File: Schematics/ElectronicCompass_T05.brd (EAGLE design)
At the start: 50.5 x 50.8 mm, 61 parts, among them Q1 FDN360P, Q2 FDN360P, Q3 FDN360P, Q4 FDN360P, U1 ATMEGA32U4, X1 USBSMD, Y1 16MHz

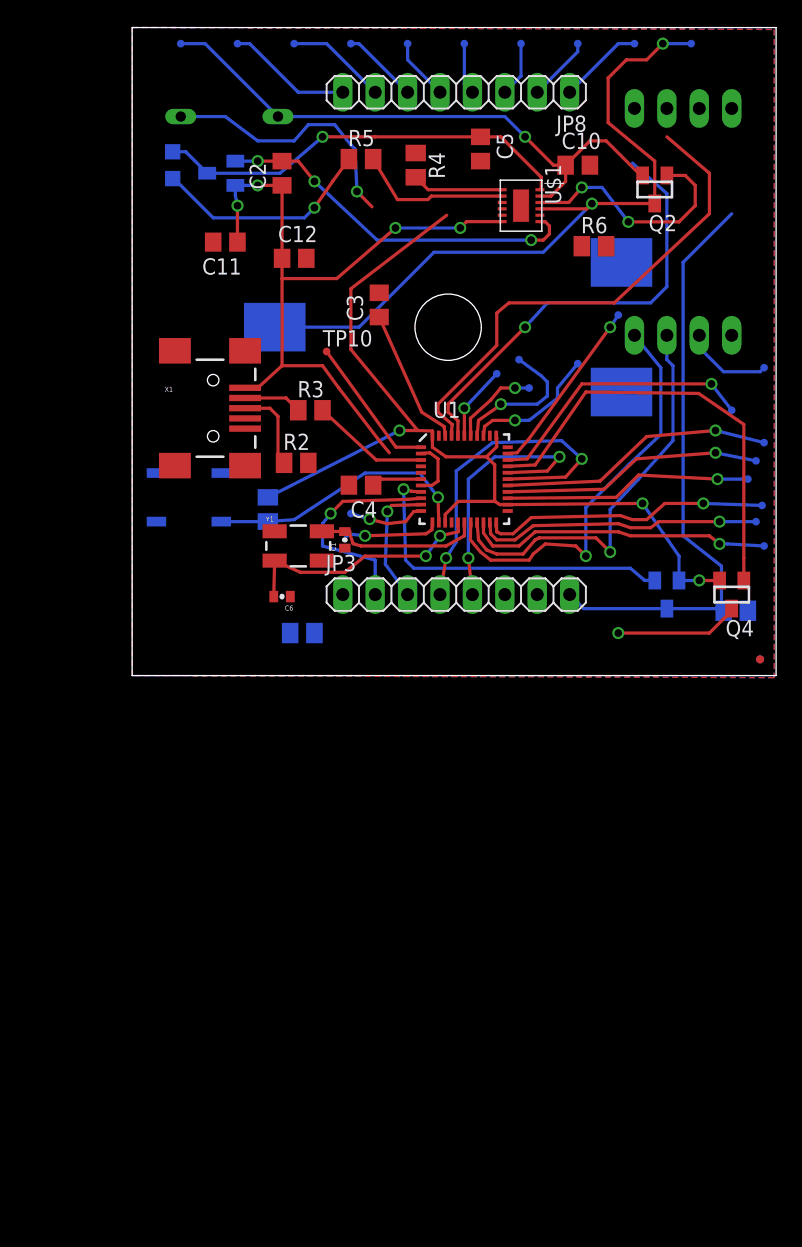
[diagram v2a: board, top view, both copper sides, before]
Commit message: Made some more updates to the schematic according to what Andrew suggested. Still need to put in the new batter header and then fix the board layout.
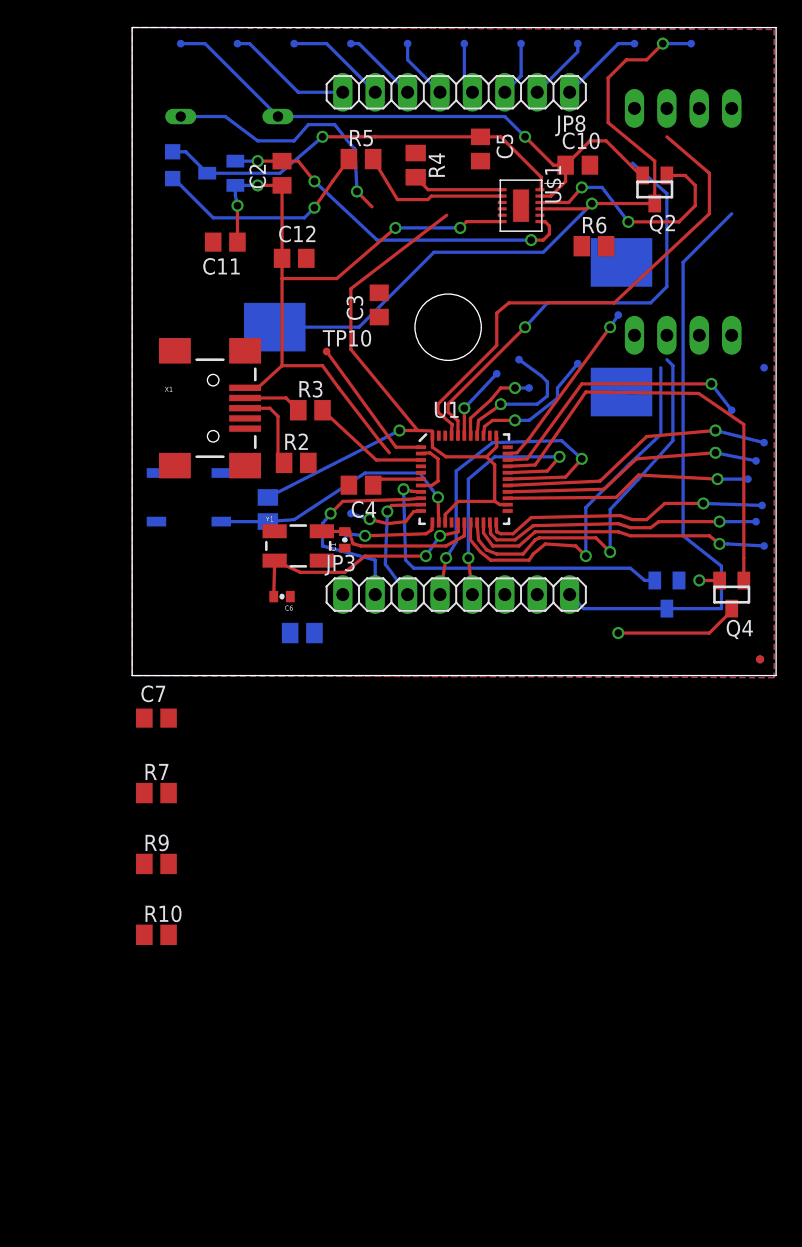
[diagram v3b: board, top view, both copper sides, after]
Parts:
- added C7: 0.1uF, rcl:C0805
- added R10: 1k, resistor:M0805
- added R9: 10k, resistor:M0805
- R7: value 1M -> 1k; device rcl:M0805 -> resistor:M0805
- R8: value 1M -> 10k
- moved R7 47.6 mm to (1.91, -9.21), flipped to the top
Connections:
- net AREF renamed N$38
- new net N$11: C7.2, U1.14, U1.24, U1.34, U1.44
- net DRDY: now also JP1.2; no longer JP1.3
- net GND: now also JP1.1, R9.1; no longer JP1.4, R7.1
- net N$26: now also R10.1
- net N$37: now also R7.2
- net SCL: now also JP1.4; no longer JP1.1
- net SDA: now also JP1.3; no longer JP1.2
- net VCC: now also C7.1, R10.2, R7.1; no longer U1.14, U1.24, U1.34, U1.44
- net VCC': now also R9.2; no longer R7.2
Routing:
- net VCC: track 95.6 -> 59.1 mm, vias 4 -> 3
- net N$11: track 0.00 -> 17.2 mm
- net N$38: track 11.0 -> 0.00 mm
- net DRDY: track 6.95 -> 0.00 mm
- net SCL: track 32.5 -> 29.2 mm
- net SDA: track 32.2 -> 30.3 mm

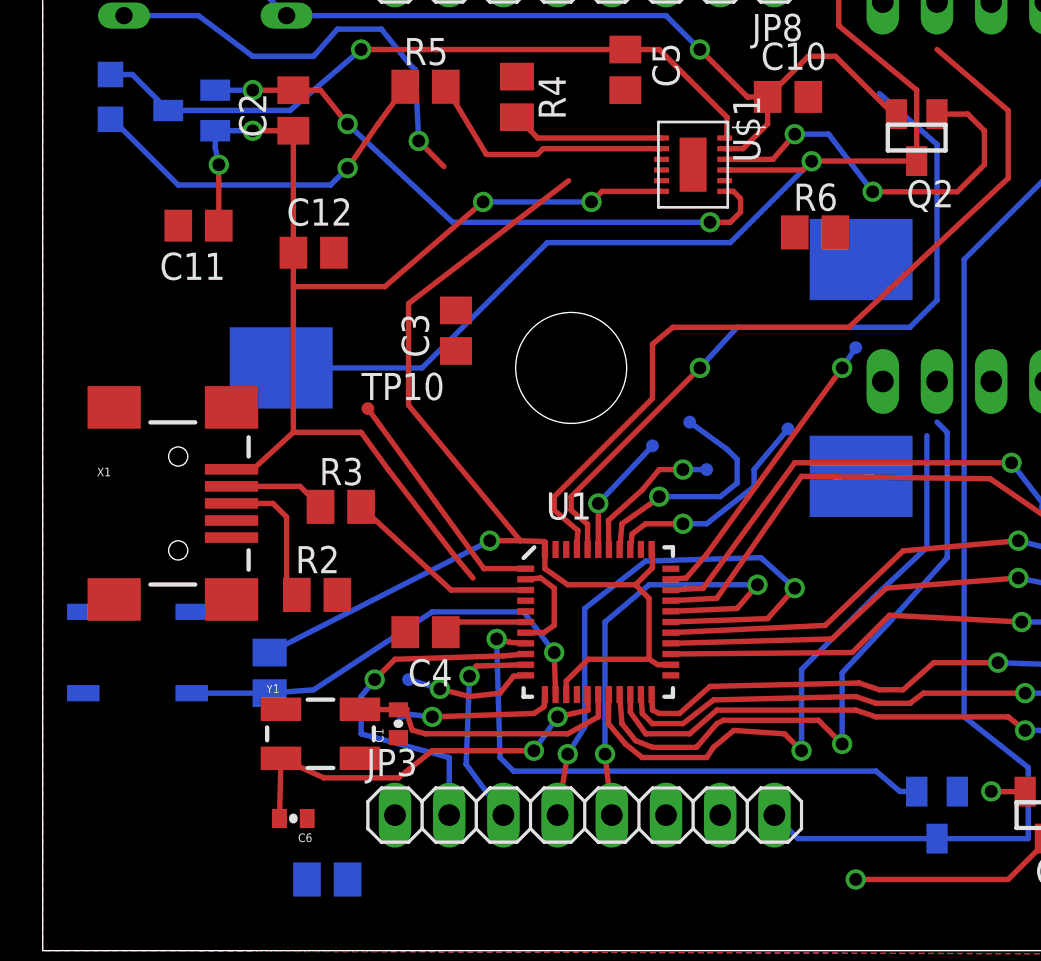
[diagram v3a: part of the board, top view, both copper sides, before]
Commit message: Made some updates to the schem and board.  Still a lot of issues with the board layout that need to be worked out.
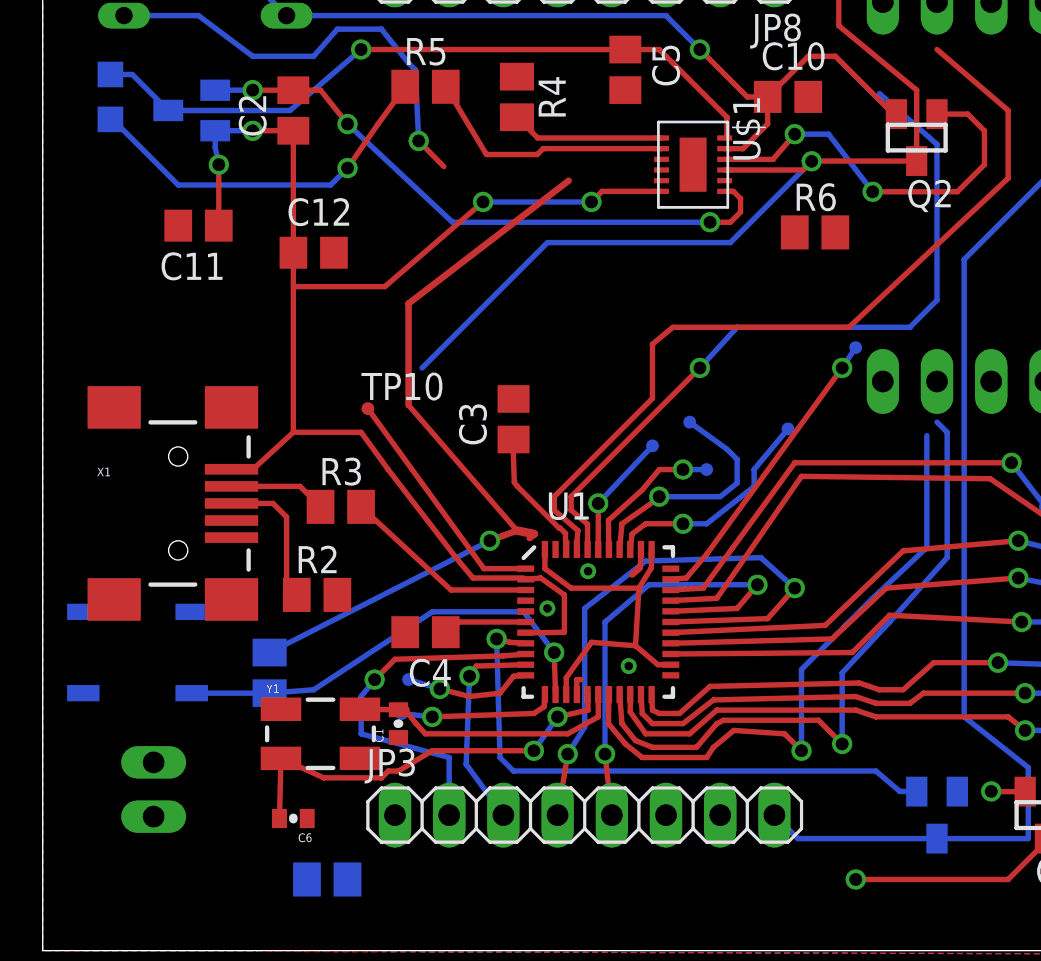
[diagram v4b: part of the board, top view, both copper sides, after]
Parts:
- removed G1: SL340SM, battery:SL-340/SM3.6V
- added JP4: BATT, pinhead:1X02
- moved C3 4.95 mm to (22.1, 24.9)
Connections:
- net GND: now also JP4.2; no longer G1.-
- net N$5: now also JP4.1; no longer G1.+
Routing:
- net N$5: track 57.2 -> 50.6 mm
- net N$43: track 0.00 -> 5.38 mm
- net VBUS: track 61.2 -> 64.6 mm
- net GND: track 0.00 -> 1.81 mm, vias 0 -> 3
- net VCC: track 59.1 -> 58.6 mm

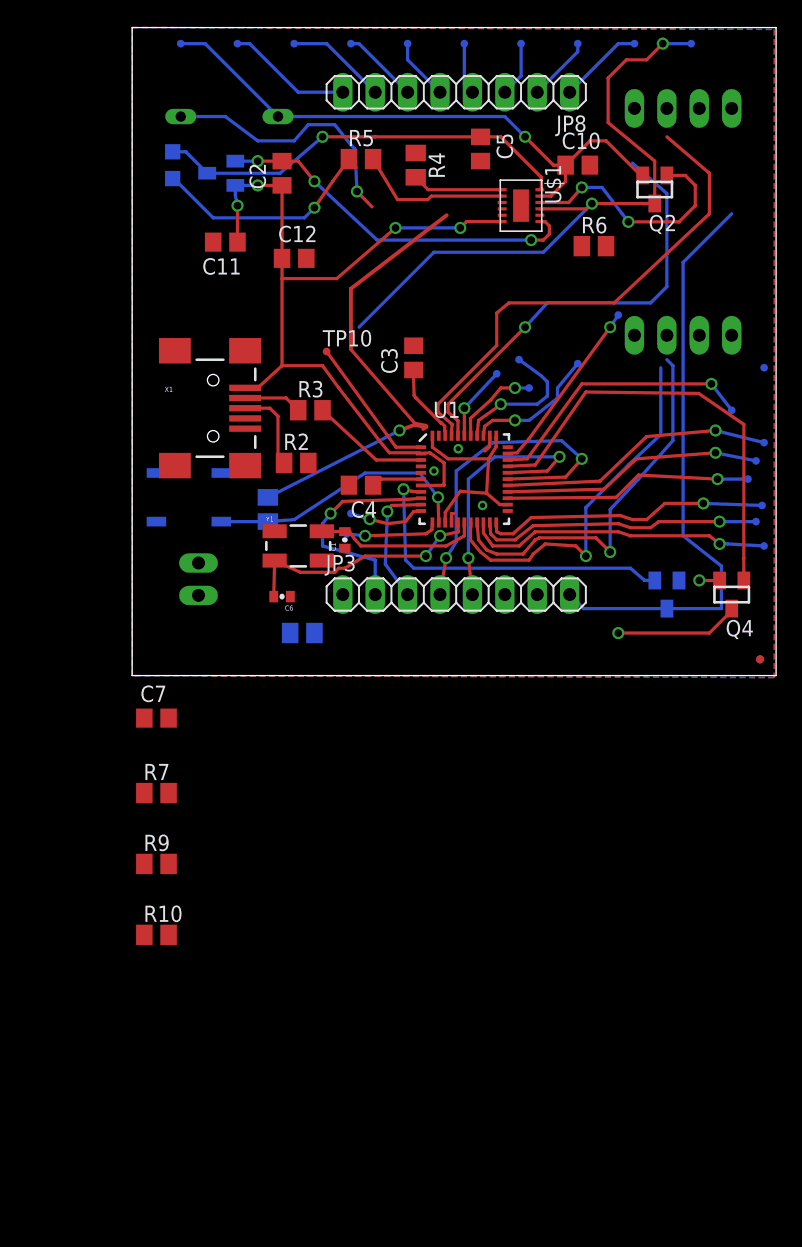
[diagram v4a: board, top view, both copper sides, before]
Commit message: Fixed transistor switches
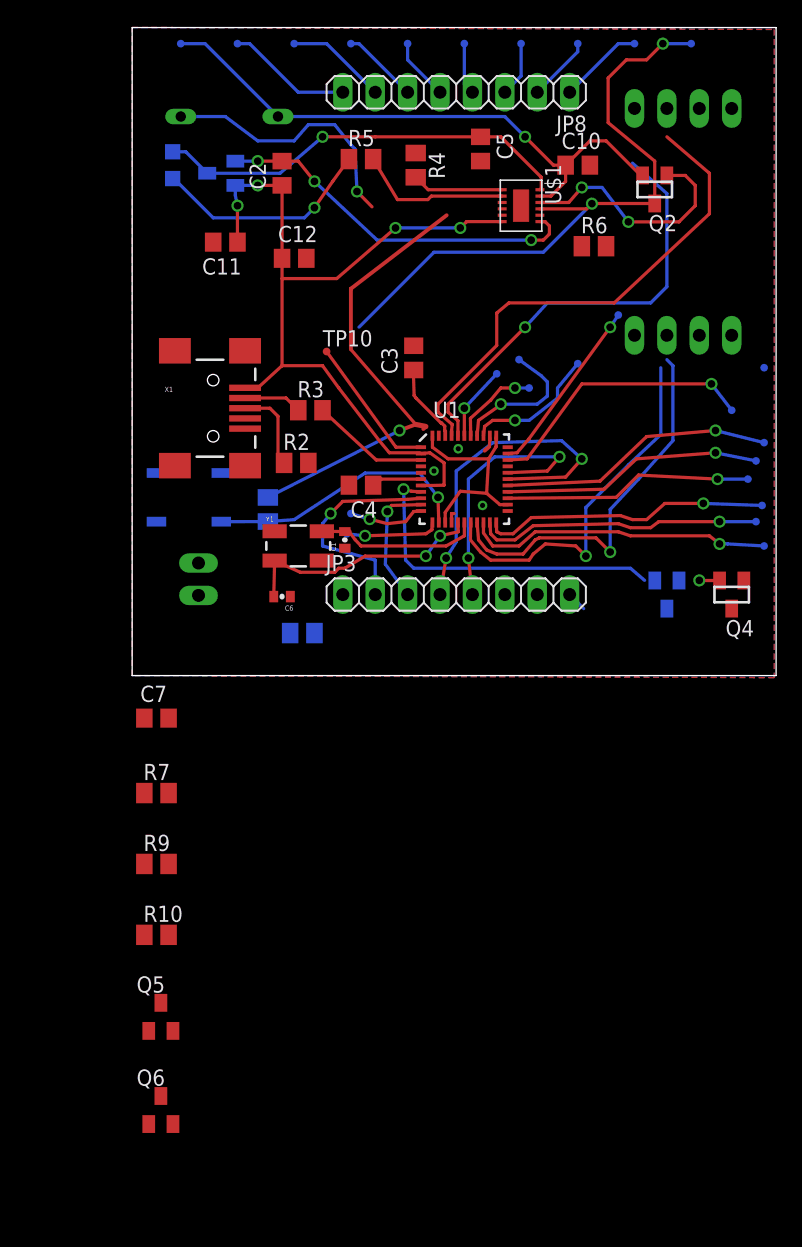
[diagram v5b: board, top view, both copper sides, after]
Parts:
- removed JP6, JP7: FIDUCIALUFIDUCIAL, SparkFun:MICRO-FIDUCIAL
- added Q5, Q6: BC817-16LT1SMD, transistor-npn:SOT23-BEC
- R10, R7: value 1k -> 1M
- R8, R9: value 10k -> 1k
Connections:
- new net N$44: Q6.B, U1.30
- new net N$45: Q3.1, Q5.C, R7.1
- net GND: now also Q5.E, Q6.E
- net N$26: now also Q6.C, R10.2; no longer R10.1, U1.30
- net N$37: now also Q5.B; no longer Q3.1, R7.2
- net VCC: now also R10.1, R7.2; no longer R10.2, R7.1
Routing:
- net VCC': track 46.3 -> 1.56 mm
- net N$26: track 34.5 -> 0.00 mm
- net LCD_BKLT: track 10.6 -> 0.79 mm, vias 1 -> 0
- net N$37: track 27.1 -> 26.3 mm
